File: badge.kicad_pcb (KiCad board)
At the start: 4 copper layers, 100 x 100 mm, 604 parts, among them IC1 SAMD21G18A-MU, J1 USB_C, J2 DEBUG, J3 LiPo 1S, Q1 3412, Q10 3412, Q11 3412, Q12 3412, Q13 3412, Q14 3412, Q15 3412, Q16 3412, Q2 3412, Q3 3412, Q4 3412, Q5 3412, Q6 3412, Q7 3412, Q8 3412, Q9 3412, SW1 A, SW2 B, SW3 X, SW4 Y, SW5 RESET, U1 74HC595, U2 74HC595, U3 TLC59025, U4 TLC59025, U5 GD25Q32C, U6 DW01, U7 TLV62569DBV, U8 PM8205A, U9 HX4054A, X1 #badgelife

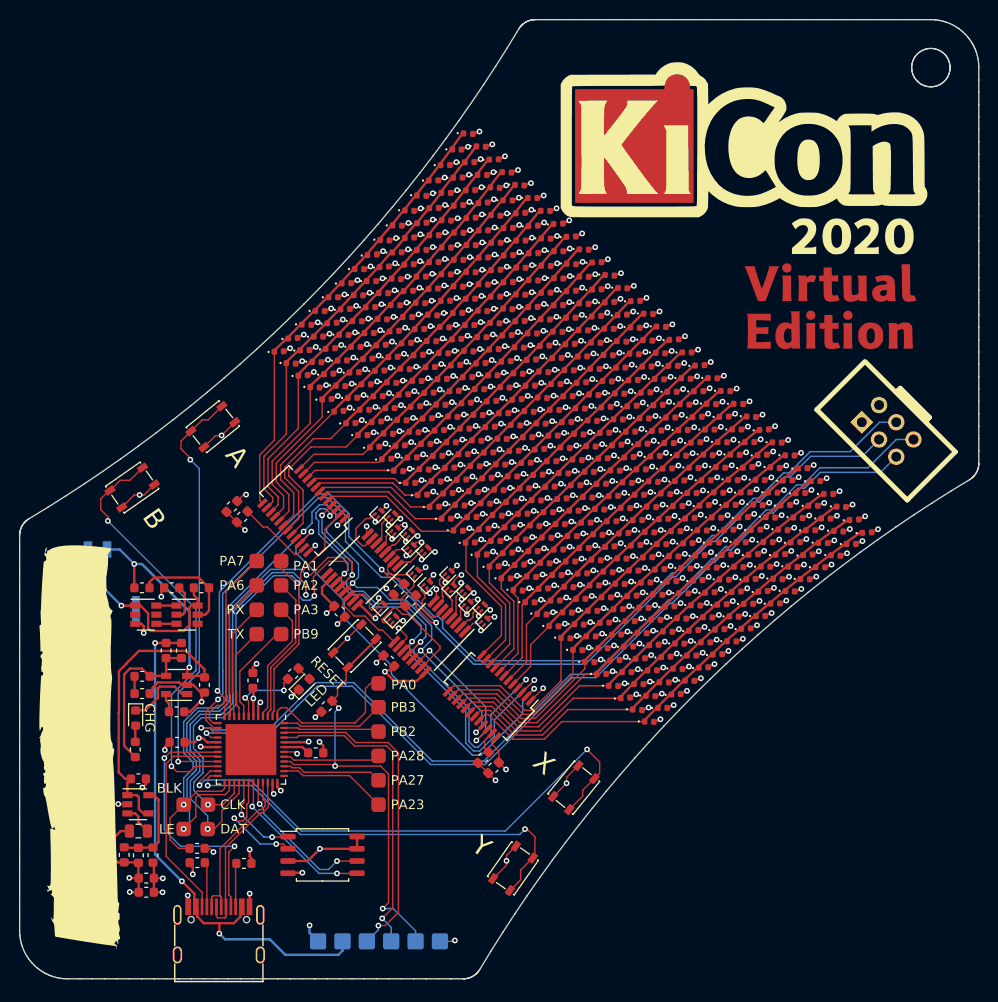
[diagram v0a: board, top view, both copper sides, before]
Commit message: Changed FETs to SOT-23 and buttons to something that is more boring
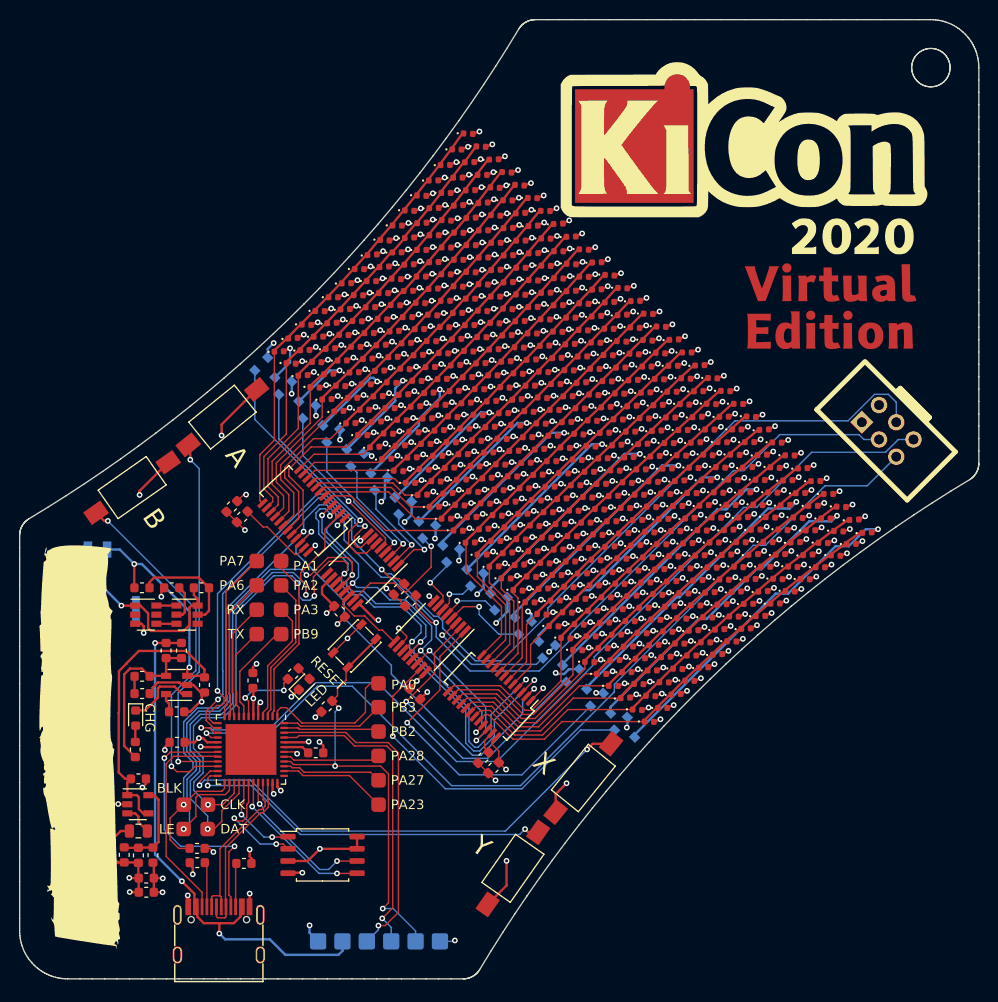
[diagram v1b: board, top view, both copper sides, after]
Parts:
- Q1, Q10, Q11, Q12, Q13, Q14, Q15, Q16, Q2, Q3, Q4, Q5, Q6, Q7, Q8, Q9: footprint Package_TO_SOT_SMD:SOT-883 -> Package_TO_SOT_SMD:SOT-23; moved to B.Cu
- R9: value 4.7K -> 4.7k
- SW1, SW2, SW3, SW4: footprint Button_Switch_SMD:SW_SPST_PTS810 -> tom-mechanical:SW_SPST_SMD_2PIN_3.5x6.0
- moved Q1 27.1 mm to (113.4, 124.1), turned to -45 degrees
- moved Q16 18.8 mm to (75.9, 86.6), turned to -45 degrees
- moved Q14 16.4 mm to (78.4, 89.1), turned to -45 degrees
- moved Q3 15.3 mm to (110.9, 121.6), turned to -45 degrees
- moved Q12 14.3 mm to (80.9, 91.6), turned to -45 degrees
- moved Q5 12.9 mm to (108.4, 119.1), turned to -45 degrees
- moved Q10 11.9 mm to (83.4, 94.1), turned to -45 degrees
- moved Q7 10.7 mm to (105.9, 116.6), turned to -45 degrees
- moved Q8 9.76 mm to (85.9, 96.6), turned to -45 degrees
- moved Q2 9.03 mm to (93.4, 104.1), turned to -45 degrees
- moved Q6 9.00 mm to (88.4, 99.1), turned to -45 degrees
- moved Q9 8.31 mm to (103.4, 114.1), turned to -45 degrees
- moved Q11 6.34 mm to (100.9, 111.6), turned to -45 degrees
- moved Q13 5.87 mm to (98.4, 109.1), turned to -45 degrees
- moved C2 4.39 mm to (91.2, 120.3), turned to -45 degrees
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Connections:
- net Net-(Q1-Pad1) renamed /ISSI 12 RGB A/U1_QA
- net Net-(Q10-Pad1) renamed /ISSI 12 RGB A/U2_QE
- net Net-(Q11-Pad1) renamed /ISSI 12 RGB A/U1_QF
- net Net-(Q12-Pad1) renamed /ISSI 12 RGB A/U2_QF
- net Net-(Q13-Pad1) renamed /ISSI 12 RGB A/U1_QG
- net Net-(Q14-Pad1) renamed /ISSI 12 RGB A/U2_QG
- net Net-(Q15-Pad1) renamed /ISSI 12 RGB A/U1_QH
- net Net-(Q16-Pad1) renamed /ISSI 12 RGB A/U2_QH
- net Net-(Q2-Pad1) renamed /ISSI 12 RGB A/U2_QA
- net Net-(Q3-Pad1) renamed /ISSI 12 RGB A/U1_QB
- net Net-(Q4-Pad1) renamed /ISSI 12 RGB A/U2_QB
- net Net-(Q5-Pad1) renamed /ISSI 12 RGB A/U1_QC
- net Net-(Q6-Pad1) renamed /ISSI 12 RGB A/U2_QC
- net Net-(Q7-Pad1) renamed /ISSI 12 RGB A/U1_QD
- net Net-(Q8-Pad1) renamed /ISSI 12 RGB A/U2_QD
- net Net-(Q9-Pad1) renamed /ISSI 12 RGB A/U1_QE
- D1 pad 2: /ISSI 12 RGB A/COM_6 -> /ISSI 12 RGB A/COM_2
- D10 pad 2: /ISSI 12 RGB A/COM_6 -> /ISSI 12 RGB A/COM_2
- D100 pad 2: /ISSI 12 RGB A/COM_2 -> /ISSI 12 RGB A/COM_1
- D101 pad 2: /ISSI 12 RGB A/COM_2 -> /ISSI 12 RGB A/COM_1
- D102 pad 2: /ISSI 12 RGB A/COM_2 -> /ISSI 12 RGB A/COM_1
- D103 pad 2: /ISSI 12 RGB A/COM_2 -> /ISSI 12 RGB A/COM_1
- D104 pad 2: /ISSI 12 RGB A/COM_2 -> /ISSI 12 RGB A/COM_1
- D105 pad 2: /ISSI 12 RGB A/COM_2 -> /ISSI 12 RGB A/COM_1
- D106 pad 2: /ISSI 12 RGB A/COM_2 -> /ISSI 12 RGB A/COM_1
- D107 pad 2: /ISSI 12 RGB A/COM_2 -> /ISSI 12 RGB A/COM_1
- D108 pad 2: /ISSI 12 RGB A/COM_2 -> /ISSI 12 RGB A/COM_1
- D109 pad 2: /ISSI 12 RGB A/COM_2 -> /ISSI 12 RGB A/COM_1
- D11 pad 2: /ISSI 12 RGB A/COM_6 -> /ISSI 12 RGB A/COM_2
- D110 pad 2: /ISSI 12 RGB A/COM_2 -> /ISSI 12 RGB A/COM_1
- D111 pad 2: /ISSI 12 RGB A/COM_2 -> /ISSI 12 RGB A/COM_1
- D112 pad 2: /ISSI 12 RGB A/COM_2 -> /ISSI 12 RGB A/COM_1
- D113 pad 2: /ISSI 12 RGB A/COM_2 -> /ISSI 12 RGB A/COM_1
- D114 pad 2: /ISSI 12 RGB A/COM_2 -> /ISSI 12 RGB A/COM_1
- D115 pad 2: /ISSI 12 RGB A/COM_2 -> /ISSI 12 RGB A/COM_1
- D116 pad 2: /ISSI 12 RGB A/COM_2 -> /ISSI 12 RGB A/COM_1
- D117 pad 2: /ISSI 12 RGB A/COM_2 -> /ISSI 12 RGB A/COM_1
- D118 pad 2: /ISSI 12 RGB A/COM_2 -> /ISSI 12 RGB A/COM_1
- D119 pad 2: /ISSI 12 RGB A/COM_2 -> /ISSI 12 RGB A/COM_1
- D12 pad 2: /ISSI 12 RGB A/COM_6 -> /ISSI 12 RGB A/COM_2
- D120 pad 2: /ISSI 12 RGB A/COM_2 -> /ISSI 12 RGB A/COM_1
- D121 pad 2: /ISSI 12 RGB A/COM_2 -> /ISSI 12 RGB A/COM_1
- D122 pad 2: /ISSI 12 RGB A/COM_2 -> /ISSI 12 RGB A/COM_1
- D123 pad 2: /ISSI 12 RGB A/COM_2 -> /ISSI 12 RGB A/COM_1
- D124 pad 2: /ISSI 12 RGB A/COM_2 -> /ISSI 12 RGB A/COM_1
- D125 pad 2: /ISSI 12 RGB A/COM_2 -> /ISSI 12 RGB A/COM_1
- D126 pad 2: /ISSI 12 RGB A/COM_2 -> /ISSI 12 RGB A/COM_1
- D127 pad 2: /ISSI 12 RGB A/COM_2 -> /ISSI 12 RGB A/COM_1
- D128 pad 2: /ISSI 12 RGB A/COM_2 -> /ISSI 12 RGB A/COM_1
- D129 pad 2: /ISSI 12 RGB A/COM_3 -> /ISSI 12 RGB A/COM
- D13 pad 2: /ISSI 12 RGB A/COM_6 -> /ISSI 12 RGB A/COM_2
- D130 pad 2: /ISSI 12 RGB A/COM_3 -> /ISSI 12 RGB A/COM
- D131 pad 2: /ISSI 12 RGB A/COM_3 -> /ISSI 12 RGB A/COM
- D132 pad 2: /ISSI 12 RGB A/COM_3 -> /ISSI 12 RGB A/COM
- D133 pad 2: /ISSI 12 RGB A/COM_3 -> /ISSI 12 RGB A/COM
- D134 pad 2: /ISSI 12 RGB A/COM_3 -> /ISSI 12 RGB A/COM
- D135 pad 2: /ISSI 12 RGB A/COM_3 -> /ISSI 12 RGB A/COM
- D136 pad 2: /ISSI 12 RGB A/COM_3 -> /ISSI 12 RGB A/COM
- D137 pad 2: /ISSI 12 RGB A/COM_3 -> /ISSI 12 RGB A/COM
- D138 pad 2: /ISSI 12 RGB A/COM_3 -> /ISSI 12 RGB A/COM
- D139 pad 2: /ISSI 12 RGB A/COM_3 -> /ISSI 12 RGB A/COM
- D14 pad 2: /ISSI 12 RGB A/COM_6 -> /ISSI 12 RGB A/COM_2
- D140 pad 2: /ISSI 12 RGB A/COM_3 -> /ISSI 12 RGB A/COM
- D141 pad 2: /ISSI 12 RGB A/COM_3 -> /ISSI 12 RGB A/COM
- D142 pad 2: /ISSI 12 RGB A/COM_3 -> /ISSI 12 RGB A/COM
- D143 pad 2: /ISSI 12 RGB A/COM_3 -> /ISSI 12 RGB A/COM
- D144 pad 2: /ISSI 12 RGB A/COM_3 -> /ISSI 12 RGB A/COM
- D145 pad 2: /ISSI 12 RGB A/COM_3 -> /ISSI 12 RGB A/COM
- D146 pad 2: /ISSI 12 RGB A/COM_3 -> /ISSI 12 RGB A/COM
- D147 pad 2: /ISSI 12 RGB A/COM_3 -> /ISSI 12 RGB A/COM
- D148 pad 2: /ISSI 12 RGB A/COM_3 -> /ISSI 12 RGB A/COM
- D149 pad 2: /ISSI 12 RGB A/COM_3 -> /ISSI 12 RGB A/COM
- D15 pad 2: /ISSI 12 RGB A/COM_6 -> /ISSI 12 RGB A/COM_2
- D150 pad 2: /ISSI 12 RGB A/COM_3 -> /ISSI 12 RGB A/COM
- D151 pad 2: /ISSI 12 RGB A/COM_3 -> /ISSI 12 RGB A/COM
- D152 pad 2: /ISSI 12 RGB A/COM_3 -> /ISSI 12 RGB A/COM
- D153 pad 2: /ISSI 12 RGB A/COM_3 -> /ISSI 12 RGB A/COM
- D154 pad 2: /ISSI 12 RGB A/COM_3 -> /ISSI 12 RGB A/COM
- D155 pad 2: /ISSI 12 RGB A/COM_3 -> /ISSI 12 RGB A/COM
- D156 pad 2: /ISSI 12 RGB A/COM_3 -> /ISSI 12 RGB A/COM
- D157 pad 2: /ISSI 12 RGB A/COM_3 -> /ISSI 12 RGB A/COM
- D158 pad 2: /ISSI 12 RGB A/COM_3 -> /ISSI 12 RGB A/COM
- D159 pad 2: /ISSI 12 RGB A/COM_3 -> /ISSI 12 RGB A/COM
- D16 pad 2: /ISSI 12 RGB A/COM_6 -> /ISSI 12 RGB A/COM_2
- D160 pad 2: /ISSI 12 RGB A/COM_3 -> /ISSI 12 RGB A/COM
- D161 pad 2: /ISSI 12 RGB A/COM_8 -> /ISSI 12 RGB A/COM_14
- D162 pad 2: /ISSI 12 RGB A/COM_8 -> /ISSI 12 RGB A/COM_14
- D163 pad 2: /ISSI 12 RGB A/COM_8 -> /ISSI 12 RGB A/COM_14
- D164 pad 2: /ISSI 12 RGB A/COM_8 -> /ISSI 12 RGB A/COM_14
- D165 pad 2: /ISSI 12 RGB A/COM_8 -> /ISSI 12 RGB A/COM_14
- D166 pad 2: /ISSI 12 RGB A/COM_8 -> /ISSI 12 RGB A/COM_14
- D167 pad 2: /ISSI 12 RGB A/COM_8 -> /ISSI 12 RGB A/COM_14
- D168 pad 2: /ISSI 12 RGB A/COM_8 -> /ISSI 12 RGB A/COM_14
- D169 pad 2: /ISSI 12 RGB A/COM_8 -> /ISSI 12 RGB A/COM_14
- D17 pad 2: /ISSI 12 RGB A/COM_6 -> /ISSI 12 RGB A/COM_2
- D170 pad 2: /ISSI 12 RGB A/COM_8 -> /ISSI 12 RGB A/COM_14
- D171 pad 2: /ISSI 12 RGB A/COM_8 -> /ISSI 12 RGB A/COM_14
- D172 pad 2: /ISSI 12 RGB A/COM_8 -> /ISSI 12 RGB A/COM_14
- D173 pad 2: /ISSI 12 RGB A/COM_8 -> /ISSI 12 RGB A/COM_14
- D174 pad 2: /ISSI 12 RGB A/COM_8 -> /ISSI 12 RGB A/COM_14
- D175 pad 2: /ISSI 12 RGB A/COM_8 -> /ISSI 12 RGB A/COM_14
- D176 pad 2: /ISSI 12 RGB A/COM_8 -> /ISSI 12 RGB A/COM_14
- D177 pad 2: /ISSI 12 RGB A/COM_8 -> /ISSI 12 RGB A/COM_14
- D178 pad 2: /ISSI 12 RGB A/COM_8 -> /ISSI 12 RGB A/COM_14
- D179 pad 2: /ISSI 12 RGB A/COM_8 -> /ISSI 12 RGB A/COM_14
- D18 pad 2: /ISSI 12 RGB A/COM_6 -> /ISSI 12 RGB A/COM_2
- D180 pad 2: /ISSI 12 RGB A/COM_8 -> /ISSI 12 RGB A/COM_14
- D181 pad 2: /ISSI 12 RGB A/COM_8 -> /ISSI 12 RGB A/COM_14
- D182 pad 2: /ISSI 12 RGB A/COM_8 -> /ISSI 12 RGB A/COM_14
- D183 pad 2: /ISSI 12 RGB A/COM_8 -> /ISSI 12 RGB A/COM_14
- D184 pad 2: /ISSI 12 RGB A/COM_8 -> /ISSI 12 RGB A/COM_14
- D185 pad 2: /ISSI 12 RGB A/COM_8 -> /ISSI 12 RGB A/COM_14
- D186 pad 2: /ISSI 12 RGB A/COM_8 -> /ISSI 12 RGB A/COM_14
- D187 pad 2: /ISSI 12 RGB A/COM_8 -> /ISSI 12 RGB A/COM_14
- D188 pad 2: /ISSI 12 RGB A/COM_8 -> /ISSI 12 RGB A/COM_14
- D189 pad 2: /ISSI 12 RGB A/COM_8 -> /ISSI 12 RGB A/COM_14
- D19 pad 2: /ISSI 12 RGB A/COM_6 -> /ISSI 12 RGB A/COM_2
- D190 pad 2: /ISSI 12 RGB A/COM_8 -> /ISSI 12 RGB A/COM_14
- D191 pad 2: /ISSI 12 RGB A/COM_8 -> /ISSI 12 RGB A/COM_14
- D192 pad 2: /ISSI 12 RGB A/COM_8 -> /ISSI 12 RGB A/COM_14
- D193 pad 2: /ISSI 12 RGB A/COM_14 -> /ISSI 12 RGB A/COM_13
- D194 pad 2: /ISSI 12 RGB A/COM_14 -> /ISSI 12 RGB A/COM_13
- D195 pad 2: /ISSI 12 RGB A/COM_14 -> /ISSI 12 RGB A/COM_13
- D196 pad 2: /ISSI 12 RGB A/COM_14 -> /ISSI 12 RGB A/COM_13
- D197 pad 2: /ISSI 12 RGB A/COM_14 -> /ISSI 12 RGB A/COM_13
- D198 pad 2: /ISSI 12 RGB A/COM_14 -> /ISSI 12 RGB A/COM_13
- D199 pad 2: /ISSI 12 RGB A/COM_14 -> /ISSI 12 RGB A/COM_13
- D2 pad 2: /ISSI 12 RGB A/COM_6 -> /ISSI 12 RGB A/COM_2
- D20 pad 2: /ISSI 12 RGB A/COM_6 -> /ISSI 12 RGB A/COM_2
- D200 pad 2: /ISSI 12 RGB A/COM_14 -> /ISSI 12 RGB A/COM_13
- D201 pad 2: /ISSI 12 RGB A/COM_14 -> /ISSI 12 RGB A/COM_13
- D202 pad 2: /ISSI 12 RGB A/COM_14 -> /ISSI 12 RGB A/COM_13
- D203 pad 2: /ISSI 12 RGB A/COM_14 -> /ISSI 12 RGB A/COM_13
- D204 pad 2: /ISSI 12 RGB A/COM_14 -> /ISSI 12 RGB A/COM_13
- D205 pad 2: /ISSI 12 RGB A/COM_14 -> /ISSI 12 RGB A/COM_13
- D206 pad 2: /ISSI 12 RGB A/COM_14 -> /ISSI 12 RGB A/COM_13
- D207 pad 2: /ISSI 12 RGB A/COM_14 -> /ISSI 12 RGB A/COM_13
- D208 pad 2: /ISSI 12 RGB A/COM_14 -> /ISSI 12 RGB A/COM_13
- D209 pad 2: /ISSI 12 RGB A/COM_14 -> /ISSI 12 RGB A/COM_13
- D21 pad 2: /ISSI 12 RGB A/COM_6 -> /ISSI 12 RGB A/COM_2
- D210 pad 2: /ISSI 12 RGB A/COM_14 -> /ISSI 12 RGB A/COM_13
- D211 pad 2: /ISSI 12 RGB A/COM_14 -> /ISSI 12 RGB A/COM_13
- D212 pad 2: /ISSI 12 RGB A/COM_14 -> /ISSI 12 RGB A/COM_13
- D213 pad 2: /ISSI 12 RGB A/COM_14 -> /ISSI 12 RGB A/COM_13
- D214 pad 2: /ISSI 12 RGB A/COM_14 -> /ISSI 12 RGB A/COM_13
- D215 pad 2: /ISSI 12 RGB A/COM_14 -> /ISSI 12 RGB A/COM_13
- D216 pad 2: /ISSI 12 RGB A/COM_14 -> /ISSI 12 RGB A/COM_13
- D217 pad 2: /ISSI 12 RGB A/COM_14 -> /ISSI 12 RGB A/COM_13
- D218 pad 2: /ISSI 12 RGB A/COM_14 -> /ISSI 12 RGB A/COM_13
- D219 pad 2: /ISSI 12 RGB A/COM_14 -> /ISSI 12 RGB A/COM_13
- D22 pad 2: /ISSI 12 RGB A/COM_6 -> /ISSI 12 RGB A/COM_2
- D220 pad 2: /ISSI 12 RGB A/COM_14 -> /ISSI 12 RGB A/COM_13
- D221 pad 2: /ISSI 12 RGB A/COM_14 -> /ISSI 12 RGB A/COM_13
- D222 pad 2: /ISSI 12 RGB A/COM_14 -> /ISSI 12 RGB A/COM_13
- D223 pad 2: /ISSI 12 RGB A/COM_14 -> /ISSI 12 RGB A/COM_13
- D224 pad 2: /ISSI 12 RGB A/COM_14 -> /ISSI 12 RGB A/COM_13
- D225 pad 2: /ISSI 12 RGB A/COM_1 -> /ISSI 12 RGB A/COM_15
- D226 pad 2: /ISSI 12 RGB A/COM_1 -> /ISSI 12 RGB A/COM_15
- D227 pad 2: /ISSI 12 RGB A/COM_1 -> /ISSI 12 RGB A/COM_15
- D228 pad 2: /ISSI 12 RGB A/COM_1 -> /ISSI 12 RGB A/COM_15
- D229 pad 2: /ISSI 12 RGB A/COM_1 -> /ISSI 12 RGB A/COM_15
- D23 pad 2: /ISSI 12 RGB A/COM_6 -> /ISSI 12 RGB A/COM_2
- D230 pad 2: /ISSI 12 RGB A/COM_1 -> /ISSI 12 RGB A/COM_15
- D231 pad 2: /ISSI 12 RGB A/COM_1 -> /ISSI 12 RGB A/COM_15
- D232 pad 2: /ISSI 12 RGB A/COM_1 -> /ISSI 12 RGB A/COM_15
- D233 pad 2: /ISSI 12 RGB A/COM_1 -> /ISSI 12 RGB A/COM_15
- D234 pad 2: /ISSI 12 RGB A/COM_1 -> /ISSI 12 RGB A/COM_15
- D235 pad 2: /ISSI 12 RGB A/COM_1 -> /ISSI 12 RGB A/COM_15
- D236 pad 2: /ISSI 12 RGB A/COM_1 -> /ISSI 12 RGB A/COM_15
- D237 pad 2: /ISSI 12 RGB A/COM_1 -> /ISSI 12 RGB A/COM_15
- D238 pad 2: /ISSI 12 RGB A/COM_1 -> /ISSI 12 RGB A/COM_15
- D239 pad 2: /ISSI 12 RGB A/COM_1 -> /ISSI 12 RGB A/COM_15
- D24 pad 2: /ISSI 12 RGB A/COM_6 -> /ISSI 12 RGB A/COM_2
- D240 pad 2: /ISSI 12 RGB A/COM_1 -> /ISSI 12 RGB A/COM_15
- D241 pad 2: /ISSI 12 RGB A/COM_1 -> /ISSI 12 RGB A/COM_15
- D242 pad 2: /ISSI 12 RGB A/COM_1 -> /ISSI 12 RGB A/COM_15
- D243 pad 2: /ISSI 12 RGB A/COM_1 -> /ISSI 12 RGB A/COM_15
- D244 pad 2: /ISSI 12 RGB A/COM_1 -> /ISSI 12 RGB A/COM_15
- D245 pad 2: /ISSI 12 RGB A/COM_1 -> /ISSI 12 RGB A/COM_15
- D246 pad 2: /ISSI 12 RGB A/COM_1 -> /ISSI 12 RGB A/COM_15
- D247 pad 2: /ISSI 12 RGB A/COM_1 -> /ISSI 12 RGB A/COM_15
- D248 pad 2: /ISSI 12 RGB A/COM_1 -> /ISSI 12 RGB A/COM_15
- D249 pad 2: /ISSI 12 RGB A/COM_1 -> /ISSI 12 RGB A/COM_15
- D25 pad 2: /ISSI 12 RGB A/COM_6 -> /ISSI 12 RGB A/COM_2
- D250 pad 2: /ISSI 12 RGB A/COM_1 -> /ISSI 12 RGB A/COM_15
- D251 pad 2: /ISSI 12 RGB A/COM_1 -> /ISSI 12 RGB A/COM_15
- D252 pad 2: /ISSI 12 RGB A/COM_1 -> /ISSI 12 RGB A/COM_15
- D253 pad 2: /ISSI 12 RGB A/COM_1 -> /ISSI 12 RGB A/COM_15
- D254 pad 2: /ISSI 12 RGB A/COM_1 -> /ISSI 12 RGB A/COM_15
- D255 pad 2: /ISSI 12 RGB A/COM_1 -> /ISSI 12 RGB A/COM_15
- D256 pad 2: /ISSI 12 RGB A/COM_1 -> /ISSI 12 RGB A/COM_15
- D257 pad 2: /ISSI 12 RGB A/COM_7 -> /ISSI 12 RGB A/COM_5
- D258 pad 2: /ISSI 12 RGB A/COM_7 -> /ISSI 12 RGB A/COM_5
- D259 pad 2: /ISSI 12 RGB A/COM_7 -> /ISSI 12 RGB A/COM_5
- D26 pad 2: /ISSI 12 RGB A/COM_6 -> /ISSI 12 RGB A/COM_2
- D260 pad 2: /ISSI 12 RGB A/COM_7 -> /ISSI 12 RGB A/COM_5
- D261 pad 2: /ISSI 12 RGB A/COM_7 -> /ISSI 12 RGB A/COM_5
- D262 pad 2: /ISSI 12 RGB A/COM_7 -> /ISSI 12 RGB A/COM_5
- D263 pad 2: /ISSI 12 RGB A/COM_7 -> /ISSI 12 RGB A/COM_5
- D264 pad 2: /ISSI 12 RGB A/COM_7 -> /ISSI 12 RGB A/COM_5
- D265 pad 2: /ISSI 12 RGB A/COM_7 -> /ISSI 12 RGB A/COM_5
- D266 pad 2: /ISSI 12 RGB A/COM_7 -> /ISSI 12 RGB A/COM_5
- D267 pad 2: /ISSI 12 RGB A/COM_7 -> /ISSI 12 RGB A/COM_5
- D268 pad 2: /ISSI 12 RGB A/COM_7 -> /ISSI 12 RGB A/COM_5
- D269 pad 2: /ISSI 12 RGB A/COM_7 -> /ISSI 12 RGB A/COM_5
- D27 pad 2: /ISSI 12 RGB A/COM_6 -> /ISSI 12 RGB A/COM_2
- D270 pad 2: /ISSI 12 RGB A/COM_7 -> /ISSI 12 RGB A/COM_5
- D271 pad 2: /ISSI 12 RGB A/COM_7 -> /ISSI 12 RGB A/COM_5
- D272 pad 2: /ISSI 12 RGB A/COM_7 -> /ISSI 12 RGB A/COM_5
- D273 pad 2: /ISSI 12 RGB A/COM_7 -> /ISSI 12 RGB A/COM_5
- D274 pad 2: /ISSI 12 RGB A/COM_7 -> /ISSI 12 RGB A/COM_5
- D275 pad 2: /ISSI 12 RGB A/COM_7 -> /ISSI 12 RGB A/COM_5
- D276 pad 2: /ISSI 12 RGB A/COM_7 -> /ISSI 12 RGB A/COM_5
- D277 pad 2: /ISSI 12 RGB A/COM_7 -> /ISSI 12 RGB A/COM_5
- D278 pad 2: /ISSI 12 RGB A/COM_7 -> /ISSI 12 RGB A/COM_5
- D279 pad 2: /ISSI 12 RGB A/COM_7 -> /ISSI 12 RGB A/COM_5
- D28 pad 2: /ISSI 12 RGB A/COM_6 -> /ISSI 12 RGB A/COM_2
- D280 pad 2: /ISSI 12 RGB A/COM_7 -> /ISSI 12 RGB A/COM_5
- D281 pad 2: /ISSI 12 RGB A/COM_7 -> /ISSI 12 RGB A/COM_5
- D282 pad 2: /ISSI 12 RGB A/COM_7 -> /ISSI 12 RGB A/COM_5
- D283 pad 2: /ISSI 12 RGB A/COM_7 -> /ISSI 12 RGB A/COM_5
- D284 pad 2: /ISSI 12 RGB A/COM_7 -> /ISSI 12 RGB A/COM_5
- D285 pad 2: /ISSI 12 RGB A/COM_7 -> /ISSI 12 RGB A/COM_5
- D286 pad 2: /ISSI 12 RGB A/COM_7 -> /ISSI 12 RGB A/COM_5
- D287 pad 2: /ISSI 12 RGB A/COM_7 -> /ISSI 12 RGB A/COM_5
- D288 pad 2: /ISSI 12 RGB A/COM_7 -> /ISSI 12 RGB A/COM_5
- D289 pad 2: /ISSI 12 RGB A/COM_15 -> /ISSI 12 RGB A/COM_6
- D29 pad 2: /ISSI 12 RGB A/COM_6 -> /ISSI 12 RGB A/COM_2
- D290 pad 2: /ISSI 12 RGB A/COM_15 -> /ISSI 12 RGB A/COM_6
- D291 pad 2: /ISSI 12 RGB A/COM_15 -> /ISSI 12 RGB A/COM_6
- D292 pad 2: /ISSI 12 RGB A/COM_15 -> /ISSI 12 RGB A/COM_6
- D293 pad 2: /ISSI 12 RGB A/COM_15 -> /ISSI 12 RGB A/COM_6
- D294 pad 2: /ISSI 12 RGB A/COM_15 -> /ISSI 12 RGB A/COM_6
- D295 pad 2: /ISSI 12 RGB A/COM_15 -> /ISSI 12 RGB A/COM_6
- D296 pad 2: /ISSI 12 RGB A/COM_15 -> /ISSI 12 RGB A/COM_6
- D297 pad 2: /ISSI 12 RGB A/COM_15 -> /ISSI 12 RGB A/COM_6
- D298 pad 2: /ISSI 12 RGB A/COM_15 -> /ISSI 12 RGB A/COM_6
- D299 pad 2: /ISSI 12 RGB A/COM_15 -> /ISSI 12 RGB A/COM_6
- D3 pad 2: /ISSI 12 RGB A/COM_6 -> /ISSI 12 RGB A/COM_2
- D30 pad 2: /ISSI 12 RGB A/COM_6 -> /ISSI 12 RGB A/COM_2
- D300 pad 2: /ISSI 12 RGB A/COM_15 -> /ISSI 12 RGB A/COM_6
- D301 pad 2: /ISSI 12 RGB A/COM_15 -> /ISSI 12 RGB A/COM_6
- D302 pad 2: /ISSI 12 RGB A/COM_15 -> /ISSI 12 RGB A/COM_6
- D303 pad 2: /ISSI 12 RGB A/COM_15 -> /ISSI 12 RGB A/COM_6
- D304 pad 2: /ISSI 12 RGB A/COM_15 -> /ISSI 12 RGB A/COM_6
- D305 pad 2: /ISSI 12 RGB A/COM_15 -> /ISSI 12 RGB A/COM_6
- D306 pad 2: /ISSI 12 RGB A/COM_15 -> /ISSI 12 RGB A/COM_6
- D307 pad 2: /ISSI 12 RGB A/COM_15 -> /ISSI 12 RGB A/COM_6
- D308 pad 2: /ISSI 12 RGB A/COM_15 -> /ISSI 12 RGB A/COM_6
- D309 pad 2: /ISSI 12 RGB A/COM_15 -> /ISSI 12 RGB A/COM_6
- D31 pad 2: /ISSI 12 RGB A/COM_6 -> /ISSI 12 RGB A/COM_2
- D310 pad 2: /ISSI 12 RGB A/COM_15 -> /ISSI 12 RGB A/COM_6
- D311 pad 2: /ISSI 12 RGB A/COM_15 -> /ISSI 12 RGB A/COM_6
- D312 pad 2: /ISSI 12 RGB A/COM_15 -> /ISSI 12 RGB A/COM_6
- D313 pad 2: /ISSI 12 RGB A/COM_15 -> /ISSI 12 RGB A/COM_6
- D314 pad 2: /ISSI 12 RGB A/COM_15 -> /ISSI 12 RGB A/COM_6
- D315 pad 2: /ISSI 12 RGB A/COM_15 -> /ISSI 12 RGB A/COM_6
- D316 pad 2: /ISSI 12 RGB A/COM_15 -> /ISSI 12 RGB A/COM_6
- D317 pad 2: /ISSI 12 RGB A/COM_15 -> /ISSI 12 RGB A/COM_6
- D318 pad 2: /ISSI 12 RGB A/COM_15 -> /ISSI 12 RGB A/COM_6
- D319 pad 2: /ISSI 12 RGB A/COM_15 -> /ISSI 12 RGB A/COM_6
- D32 pad 2: /ISSI 12 RGB A/COM_6 -> /ISSI 12 RGB A/COM_2
- D320 pad 2: /ISSI 12 RGB A/COM_15 -> /ISSI 12 RGB A/COM_6
- D321 pad 2: /ISSI 12 RGB A/COM -> /ISSI 12 RGB A/COM_7
- D322 pad 2: /ISSI 12 RGB A/COM -> /ISSI 12 RGB A/COM_7
- D323 pad 2: /ISSI 12 RGB A/COM -> /ISSI 12 RGB A/COM_7
- D324 pad 2: /ISSI 12 RGB A/COM -> /ISSI 12 RGB A/COM_7
- D325 pad 2: /ISSI 12 RGB A/COM -> /ISSI 12 RGB A/COM_7
- D326 pad 2: /ISSI 12 RGB A/COM -> /ISSI 12 RGB A/COM_7
- D327 pad 2: /ISSI 12 RGB A/COM -> /ISSI 12 RGB A/COM_7
- D328 pad 2: /ISSI 12 RGB A/COM -> /ISSI 12 RGB A/COM_7
- D329 pad 2: /ISSI 12 RGB A/COM -> /ISSI 12 RGB A/COM_7
- D33 pad 2: /ISSI 12 RGB A/COM_5 -> /ISSI 12 RGB A/COM_3
- D330 pad 2: /ISSI 12 RGB A/COM -> /ISSI 12 RGB A/COM_7
- D331 pad 2: /ISSI 12 RGB A/COM -> /ISSI 12 RGB A/COM_7
- D332 pad 2: /ISSI 12 RGB A/COM -> /ISSI 12 RGB A/COM_7
- D333 pad 2: /ISSI 12 RGB A/COM -> /ISSI 12 RGB A/COM_7
- D334 pad 2: /ISSI 12 RGB A/COM -> /ISSI 12 RGB A/COM_7
- D335 pad 2: /ISSI 12 RGB A/COM -> /ISSI 12 RGB A/COM_7
- D336 pad 2: /ISSI 12 RGB A/COM -> /ISSI 12 RGB A/COM_7
- D337 pad 2: /ISSI 12 RGB A/COM -> /ISSI 12 RGB A/COM_7
- D338 pad 2: /ISSI 12 RGB A/COM -> /ISSI 12 RGB A/COM_7
- D339 pad 2: /ISSI 12 RGB A/COM -> /ISSI 12 RGB A/COM_7
- D34 pad 2: /ISSI 12 RGB A/COM_5 -> /ISSI 12 RGB A/COM_3
- D340 pad 2: /ISSI 12 RGB A/COM -> /ISSI 12 RGB A/COM_7
- D341 pad 2: /ISSI 12 RGB A/COM -> /ISSI 12 RGB A/COM_7
- D342 pad 2: /ISSI 12 RGB A/COM -> /ISSI 12 RGB A/COM_7
- D343 pad 2: /ISSI 12 RGB A/COM -> /ISSI 12 RGB A/COM_7
- D344 pad 2: /ISSI 12 RGB A/COM -> /ISSI 12 RGB A/COM_7
- D345 pad 2: /ISSI 12 RGB A/COM -> /ISSI 12 RGB A/COM_7
- D346 pad 2: /ISSI 12 RGB A/COM -> /ISSI 12 RGB A/COM_7
- D347 pad 2: /ISSI 12 RGB A/COM -> /ISSI 12 RGB A/COM_7
- D348 pad 2: /ISSI 12 RGB A/COM -> /ISSI 12 RGB A/COM_7
- D349 pad 2: /ISSI 12 RGB A/COM -> /ISSI 12 RGB A/COM_7
- D35 pad 2: /ISSI 12 RGB A/COM_5 -> /ISSI 12 RGB A/COM_3
- D350 pad 2: /ISSI 12 RGB A/COM -> /ISSI 12 RGB A/COM_7
- D351 pad 2: /ISSI 12 RGB A/COM -> /ISSI 12 RGB A/COM_7
- D352 pad 2: /ISSI 12 RGB A/COM -> /ISSI 12 RGB A/COM_7
- D353 pad 2: /ISSI 12 RGB A/COM_12 -> /ISSI 12 RGB A/COM_8
- D354 pad 2: /ISSI 12 RGB A/COM_12 -> /ISSI 12 RGB A/COM_8
- D355 pad 2: /ISSI 12 RGB A/COM_12 -> /ISSI 12 RGB A/COM_8
- D356 pad 2: /ISSI 12 RGB A/COM_12 -> /ISSI 12 RGB A/COM_8
- D357 pad 2: /ISSI 12 RGB A/COM_12 -> /ISSI 12 RGB A/COM_8
- D358 pad 2: /ISSI 12 RGB A/COM_12 -> /ISSI 12 RGB A/COM_8
- D359 pad 2: /ISSI 12 RGB A/COM_12 -> /ISSI 12 RGB A/COM_8
- D36 pad 2: /ISSI 12 RGB A/COM_5 -> /ISSI 12 RGB A/COM_3
- D360 pad 2: /ISSI 12 RGB A/COM_12 -> /ISSI 12 RGB A/COM_8
- D361 pad 2: /ISSI 12 RGB A/COM_12 -> /ISSI 12 RGB A/COM_8
- D362 pad 2: /ISSI 12 RGB A/COM_12 -> /ISSI 12 RGB A/COM_8
- D363 pad 2: /ISSI 12 RGB A/COM_12 -> /ISSI 12 RGB A/COM_8
- D364 pad 2: /ISSI 12 RGB A/COM_12 -> /ISSI 12 RGB A/COM_8
- D365 pad 2: /ISSI 12 RGB A/COM_12 -> /ISSI 12 RGB A/COM_8
- D366 pad 2: /ISSI 12 RGB A/COM_12 -> /ISSI 12 RGB A/COM_8
- D367 pad 2: /ISSI 12 RGB A/COM_12 -> /ISSI 12 RGB A/COM_8
- D368 pad 2: /ISSI 12 RGB A/COM_12 -> /ISSI 12 RGB A/COM_8
- D369 pad 2: /ISSI 12 RGB A/COM_12 -> /ISSI 12 RGB A/COM_8
- D37 pad 2: /ISSI 12 RGB A/COM_5 -> /ISSI 12 RGB A/COM_3
- D370 pad 2: /ISSI 12 RGB A/COM_12 -> /ISSI 12 RGB A/COM_8
- D371 pad 2: /ISSI 12 RGB A/COM_12 -> /ISSI 12 RGB A/COM_8
- D372 pad 2: /ISSI 12 RGB A/COM_12 -> /ISSI 12 RGB A/COM_8
- D373 pad 2: /ISSI 12 RGB A/COM_12 -> /ISSI 12 RGB A/COM_8
- D374 pad 2: /ISSI 12 RGB A/COM_12 -> /ISSI 12 RGB A/COM_8
- D375 pad 2: /ISSI 12 RGB A/COM_12 -> /ISSI 12 RGB A/COM_8
- D376 pad 2: /ISSI 12 RGB A/COM_12 -> /ISSI 12 RGB A/COM_8
- D377 pad 2: /ISSI 12 RGB A/COM_12 -> /ISSI 12 RGB A/COM_8
- D378 pad 2: /ISSI 12 RGB A/COM_12 -> /ISSI 12 RGB A/COM_8
- D379 pad 2: /ISSI 12 RGB A/COM_12 -> /ISSI 12 RGB A/COM_8
- D38 pad 2: /ISSI 12 RGB A/COM_5 -> /ISSI 12 RGB A/COM_3
- D380 pad 2: /ISSI 12 RGB A/COM_12 -> /ISSI 12 RGB A/COM_8
- D381 pad 2: /ISSI 12 RGB A/COM_12 -> /ISSI 12 RGB A/COM_8
- D382 pad 2: /ISSI 12 RGB A/COM_12 -> /ISSI 12 RGB A/COM_8
- D383 pad 2: /ISSI 12 RGB A/COM_12 -> /ISSI 12 RGB A/COM_8
- D384 pad 2: /ISSI 12 RGB A/COM_12 -> /ISSI 12 RGB A/COM_8
- D385 pad 2: /ISSI 12 RGB A/COM_13 -> /ISSI 12 RGB A/COM_9
- D386 pad 2: /ISSI 12 RGB A/COM_13 -> /ISSI 12 RGB A/COM_9
- D387 pad 2: /ISSI 12 RGB A/COM_13 -> /ISSI 12 RGB A/COM_9
- D388 pad 2: /ISSI 12 RGB A/COM_13 -> /ISSI 12 RGB A/COM_9
- D389 pad 2: /ISSI 12 RGB A/COM_13 -> /ISSI 12 RGB A/COM_9
- D39 pad 2: /ISSI 12 RGB A/COM_5 -> /ISSI 12 RGB A/COM_3
- D390 pad 2: /ISSI 12 RGB A/COM_13 -> /ISSI 12 RGB A/COM_9
- D391 pad 2: /ISSI 12 RGB A/COM_13 -> /ISSI 12 RGB A/COM_9
- D392 pad 2: /ISSI 12 RGB A/COM_13 -> /ISSI 12 RGB A/COM_9
- D393 pad 2: /ISSI 12 RGB A/COM_13 -> /ISSI 12 RGB A/COM_9
- D394 pad 2: /ISSI 12 RGB A/COM_13 -> /ISSI 12 RGB A/COM_9
- D395 pad 2: /ISSI 12 RGB A/COM_13 -> /ISSI 12 RGB A/COM_9
- D396 pad 2: /ISSI 12 RGB A/COM_13 -> /ISSI 12 RGB A/COM_9
- D397 pad 2: /ISSI 12 RGB A/COM_13 -> /ISSI 12 RGB A/COM_9
- D398 pad 2: /ISSI 12 RGB A/COM_13 -> /ISSI 12 RGB A/COM_9
- D399 pad 2: /ISSI 12 RGB A/COM_13 -> /ISSI 12 RGB A/COM_9
- D4 pad 2: /ISSI 12 RGB A/COM_6 -> /ISSI 12 RGB A/COM_2
- D40 pad 2: /ISSI 12 RGB A/COM_5 -> /ISSI 12 RGB A/COM_3
- D400 pad 2: /ISSI 12 RGB A/COM_13 -> /ISSI 12 RGB A/COM_9
- D401 pad 2: /ISSI 12 RGB A/COM_13 -> /ISSI 12 RGB A/COM_9
- D402 pad 2: /ISSI 12 RGB A/COM_13 -> /ISSI 12 RGB A/COM_9
- D403 pad 2: /ISSI 12 RGB A/COM_13 -> /ISSI 12 RGB A/COM_9
- D404 pad 2: /ISSI 12 RGB A/COM_13 -> /ISSI 12 RGB A/COM_9
- D405 pad 2: /ISSI 12 RGB A/COM_13 -> /ISSI 12 RGB A/COM_9
- D406 pad 2: /ISSI 12 RGB A/COM_13 -> /ISSI 12 RGB A/COM_9
- D407 pad 2: /ISSI 12 RGB A/COM_13 -> /ISSI 12 RGB A/COM_9
- D408 pad 2: /ISSI 12 RGB A/COM_13 -> /ISSI 12 RGB A/COM_9
- D409 pad 2: /ISSI 12 RGB A/COM_13 -> /ISSI 12 RGB A/COM_9
- D41 pad 2: /ISSI 12 RGB A/COM_5 -> /ISSI 12 RGB A/COM_3
- D410 pad 2: /ISSI 12 RGB A/COM_13 -> /ISSI 12 RGB A/COM_9
- D411 pad 2: /ISSI 12 RGB A/COM_13 -> /ISSI 12 RGB A/COM_9
- D412 pad 2: /ISSI 12 RGB A/COM_13 -> /ISSI 12 RGB A/COM_9
- D413 pad 2: /ISSI 12 RGB A/COM_13 -> /ISSI 12 RGB A/COM_9
- D414 pad 2: /ISSI 12 RGB A/COM_13 -> /ISSI 12 RGB A/COM_9
- D415 pad 2: /ISSI 12 RGB A/COM_13 -> /ISSI 12 RGB A/COM_9
- D416 pad 2: /ISSI 12 RGB A/COM_13 -> /ISSI 12 RGB A/COM_9
- D417 pad 2: /ISSI 12 RGB A/COM_9 -> /ISSI 12 RGB A/COM_10
- D418 pad 2: /ISSI 12 RGB A/COM_9 -> /ISSI 12 RGB A/COM_10
- D419 pad 2: /ISSI 12 RGB A/COM_9 -> /ISSI 12 RGB A/COM_10
- D42 pad 2: /ISSI 12 RGB A/COM_5 -> /ISSI 12 RGB A/COM_3
- D420 pad 2: /ISSI 12 RGB A/COM_9 -> /ISSI 12 RGB A/COM_10
- D421 pad 2: /ISSI 12 RGB A/COM_9 -> /ISSI 12 RGB A/COM_10
- D422 pad 2: /ISSI 12 RGB A/COM_9 -> /ISSI 12 RGB A/COM_10
- D423 pad 2: /ISSI 12 RGB A/COM_9 -> /ISSI 12 RGB A/COM_10
- D424 pad 2: /ISSI 12 RGB A/COM_9 -> /ISSI 12 RGB A/COM_10
- D425 pad 2: /ISSI 12 RGB A/COM_9 -> /ISSI 12 RGB A/COM_10
- D426 pad 2: /ISSI 12 RGB A/COM_9 -> /ISSI 12 RGB A/COM_10
- D427 pad 2: /ISSI 12 RGB A/COM_9 -> /ISSI 12 RGB A/COM_10
- D428 pad 2: /ISSI 12 RGB A/COM_9 -> /ISSI 12 RGB A/COM_10
- D429 pad 2: /ISSI 12 RGB A/COM_9 -> /ISSI 12 RGB A/COM_10
- D43 pad 2: /ISSI 12 RGB A/COM_5 -> /ISSI 12 RGB A/COM_3
- D430 pad 2: /ISSI 12 RGB A/COM_9 -> /ISSI 12 RGB A/COM_10
- D431 pad 2: /ISSI 12 RGB A/COM_9 -> /ISSI 12 RGB A/COM_10
- D432 pad 2: /ISSI 12 RGB A/COM_9 -> /ISSI 12 RGB A/COM_10
- D433 pad 2: /ISSI 12 RGB A/COM_9 -> /ISSI 12 RGB A/COM_10
- D434 pad 2: /ISSI 12 RGB A/COM_9 -> /ISSI 12 RGB A/COM_10
- D435 pad 2: /ISSI 12 RGB A/COM_9 -> /ISSI 12 RGB A/COM_10
- D436 pad 2: /ISSI 12 RGB A/COM_9 -> /ISSI 12 RGB A/COM_10
- D437 pad 2: /ISSI 12 RGB A/COM_9 -> /ISSI 12 RGB A/COM_10
- D438 pad 2: /ISSI 12 RGB A/COM_9 -> /ISSI 12 RGB A/COM_10
- D439 pad 2: /ISSI 12 RGB A/COM_9 -> /ISSI 12 RGB A/COM_10
- D44 pad 2: /ISSI 12 RGB A/COM_5 -> /ISSI 12 RGB A/COM_3
- D440 pad 2: /ISSI 12 RGB A/COM_9 -> /ISSI 12 RGB A/COM_10
- D441 pad 2: /ISSI 12 RGB A/COM_9 -> /ISSI 12 RGB A/COM_10
- D442 pad 2: /ISSI 12 RGB A/COM_9 -> /ISSI 12 RGB A/COM_10
- D443 pad 2: /ISSI 12 RGB A/COM_9 -> /ISSI 12 RGB A/COM_10
- D444 pad 2: /ISSI 12 RGB A/COM_9 -> /ISSI 12 RGB A/COM_10
- D445 pad 2: /ISSI 12 RGB A/COM_9 -> /ISSI 12 RGB A/COM_10
- D446 pad 2: /ISSI 12 RGB A/COM_9 -> /ISSI 12 RGB A/COM_10
- D447 pad 2: /ISSI 12 RGB A/COM_9 -> /ISSI 12 RGB A/COM_10
- D448 pad 2: /ISSI 12 RGB A/COM_9 -> /ISSI 12 RGB A/COM_10
- D449 pad 2: /ISSI 12 RGB A/COM_10 -> /ISSI 12 RGB A/COM_11
- D45 pad 2: /ISSI 12 RGB A/COM_5 -> /ISSI 12 RGB A/COM_3
- D450 pad 2: /ISSI 12 RGB A/COM_10 -> /ISSI 12 RGB A/COM_11
- D451 pad 2: /ISSI 12 RGB A/COM_10 -> /ISSI 12 RGB A/COM_11
- D452 pad 2: /ISSI 12 RGB A/COM_10 -> /ISSI 12 RGB A/COM_11
- D453 pad 2: /ISSI 12 RGB A/COM_10 -> /ISSI 12 RGB A/COM_11
- D454 pad 2: /ISSI 12 RGB A/COM_10 -> /ISSI 12 RGB A/COM_11
- D455 pad 2: /ISSI 12 RGB A/COM_10 -> /ISSI 12 RGB A/COM_11
- D456 pad 2: /ISSI 12 RGB A/COM_10 -> /ISSI 12 RGB A/COM_11
- D457 pad 2: /ISSI 12 RGB A/COM_10 -> /ISSI 12 RGB A/COM_11
- D458 pad 2: /ISSI 12 RGB A/COM_10 -> /ISSI 12 RGB A/COM_11
- D459 pad 2: /ISSI 12 RGB A/COM_10 -> /ISSI 12 RGB A/COM_11
- D46 pad 2: /ISSI 12 RGB A/COM_5 -> /ISSI 12 RGB A/COM_3
- D460 pad 2: /ISSI 12 RGB A/COM_10 -> /ISSI 12 RGB A/COM_11
- D461 pad 2: /ISSI 12 RGB A/COM_10 -> /ISSI 12 RGB A/COM_11
- D462 pad 2: /ISSI 12 RGB A/COM_10 -> /ISSI 12 RGB A/COM_11
- D463 pad 2: /ISSI 12 RGB A/COM_10 -> /ISSI 12 RGB A/COM_11
- D464 pad 2: /ISSI 12 RGB A/COM_10 -> /ISSI 12 RGB A/COM_11
- D465 pad 2: /ISSI 12 RGB A/COM_10 -> /ISSI 12 RGB A/COM_11
- D466 pad 2: /ISSI 12 RGB A/COM_10 -> /ISSI 12 RGB A/COM_11
- D467 pad 2: /ISSI 12 RGB A/COM_10 -> /ISSI 12 RGB A/COM_11
- D468 pad 2: /ISSI 12 RGB A/COM_10 -> /ISSI 12 RGB A/COM_11
- D469 pad 2: /ISSI 12 RGB A/COM_10 -> /ISSI 12 RGB A/COM_11
- D47 pad 2: /ISSI 12 RGB A/COM_5 -> /ISSI 12 RGB A/COM_3
- D470 pad 2: /ISSI 12 RGB A/COM_10 -> /ISSI 12 RGB A/COM_11
- D471 pad 2: /ISSI 12 RGB A/COM_10 -> /ISSI 12 RGB A/COM_11
- D472 pad 2: /ISSI 12 RGB A/COM_10 -> /ISSI 12 RGB A/COM_11
- D473 pad 2: /ISSI 12 RGB A/COM_10 -> /ISSI 12 RGB A/COM_11
- D474 pad 2: /ISSI 12 RGB A/COM_10 -> /ISSI 12 RGB A/COM_11
- D475 pad 2: /ISSI 12 RGB A/COM_10 -> /ISSI 12 RGB A/COM_11
- D476 pad 2: /ISSI 12 RGB A/COM_10 -> /ISSI 12 RGB A/COM_11
- D477 pad 2: /ISSI 12 RGB A/COM_10 -> /ISSI 12 RGB A/COM_11
- D478 pad 2: /ISSI 12 RGB A/COM_10 -> /ISSI 12 RGB A/COM_11
- D479 pad 2: /ISSI 12 RGB A/COM_10 -> /ISSI 12 RGB A/COM_11
- D48 pad 2: /ISSI 12 RGB A/COM_5 -> /ISSI 12 RGB A/COM_3
- D480 pad 2: /ISSI 12 RGB A/COM_10 -> /ISSI 12 RGB A/COM_11
- D481 pad 2: /ISSI 12 RGB A/COM_11 -> /ISSI 12 RGB A/COM_12
- D482 pad 2: /ISSI 12 RGB A/COM_11 -> /ISSI 12 RGB A/COM_12
- D483 pad 2: /ISSI 12 RGB A/COM_11 -> /ISSI 12 RGB A/COM_12
- D484 pad 2: /ISSI 12 RGB A/COM_11 -> /ISSI 12 RGB A/COM_12
- D485 pad 2: /ISSI 12 RGB A/COM_11 -> /ISSI 12 RGB A/COM_12
- D486 pad 2: /ISSI 12 RGB A/COM_11 -> /ISSI 12 RGB A/COM_12
- D487 pad 2: /ISSI 12 RGB A/COM_11 -> /ISSI 12 RGB A/COM_12
- D488 pad 2: /ISSI 12 RGB A/COM_11 -> /ISSI 12 RGB A/COM_12
- D489 pad 2: /ISSI 12 RGB A/COM_11 -> /ISSI 12 RGB A/COM_12
- D49 pad 2: /ISSI 12 RGB A/COM_5 -> /ISSI 12 RGB A/COM_3
- D490 pad 2: /ISSI 12 RGB A/COM_11 -> /ISSI 12 RGB A/COM_12
- D491 pad 2: /ISSI 12 RGB A/COM_11 -> /ISSI 12 RGB A/COM_12
- D492 pad 2: /ISSI 12 RGB A/COM_11 -> /ISSI 12 RGB A/COM_12
- D493 pad 2: /ISSI 12 RGB A/COM_11 -> /ISSI 12 RGB A/COM_12
- D494 pad 2: /ISSI 12 RGB A/COM_11 -> /ISSI 12 RGB A/COM_12
- D495 pad 2: /ISSI 12 RGB A/COM_11 -> /ISSI 12 RGB A/COM_12
- D496 pad 2: /ISSI 12 RGB A/COM_11 -> /ISSI 12 RGB A/COM_12
- D497 pad 2: /ISSI 12 RGB A/COM_11 -> /ISSI 12 RGB A/COM_12
- D498 pad 2: /ISSI 12 RGB A/COM_11 -> /ISSI 12 RGB A/COM_12
- D499 pad 2: /ISSI 12 RGB A/COM_11 -> /ISSI 12 RGB A/COM_12
- D5 pad 2: /ISSI 12 RGB A/COM_6 -> /ISSI 12 RGB A/COM_2
- D50 pad 2: /ISSI 12 RGB A/COM_5 -> /ISSI 12 RGB A/COM_3
- D500 pad 2: /ISSI 12 RGB A/COM_11 -> /ISSI 12 RGB A/COM_12
- D501 pad 2: /ISSI 12 RGB A/COM_11 -> /ISSI 12 RGB A/COM_12
- D502 pad 2: /ISSI 12 RGB A/COM_11 -> /ISSI 12 RGB A/COM_12
- D503 pad 2: /ISSI 12 RGB A/COM_11 -> /ISSI 12 RGB A/COM_12
- D504 pad 2: /ISSI 12 RGB A/COM_11 -> /ISSI 12 RGB A/COM_12
- D505 pad 2: /ISSI 12 RGB A/COM_11 -> /ISSI 12 RGB A/COM_12
- D506 pad 2: /ISSI 12 RGB A/COM_11 -> /ISSI 12 RGB A/COM_12
- D507 pad 2: /ISSI 12 RGB A/COM_11 -> /ISSI 12 RGB A/COM_12
- D508 pad 2: /ISSI 12 RGB A/COM_11 -> /ISSI 12 RGB A/COM_12
- D509 pad 2: /ISSI 12 RGB A/COM_11 -> /ISSI 12 RGB A/COM_12
- D51 pad 2: /ISSI 12 RGB A/COM_5 -> /ISSI 12 RGB A/COM_3
- D510 pad 2: /ISSI 12 RGB A/COM_11 -> /ISSI 12 RGB A/COM_12
- D511 pad 2: /ISSI 12 RGB A/COM_11 -> /ISSI 12 RGB A/COM_12
- D512 pad 2: /ISSI 12 RGB A/COM_11 -> /ISSI 12 RGB A/COM_12
- D52 pad 2: /ISSI 12 RGB A/COM_5 -> /ISSI 12 RGB A/COM_3
- D53 pad 2: /ISSI 12 RGB A/COM_5 -> /ISSI 12 RGB A/COM_3
- D54 pad 2: /ISSI 12 RGB A/COM_5 -> /ISSI 12 RGB A/COM_3
- D55 pad 2: /ISSI 12 RGB A/COM_5 -> /ISSI 12 RGB A/COM_3
- D56 pad 2: /ISSI 12 RGB A/COM_5 -> /ISSI 12 RGB A/COM_3
- D57 pad 2: /ISSI 12 RGB A/COM_5 -> /ISSI 12 RGB A/COM_3
- D58 pad 2: /ISSI 12 RGB A/COM_5 -> /ISSI 12 RGB A/COM_3
- D59 pad 2: /ISSI 12 RGB A/COM_5 -> /ISSI 12 RGB A/COM_3
- D6 pad 2: /ISSI 12 RGB A/COM_6 -> /ISSI 12 RGB A/COM_2
- D60 pad 2: /ISSI 12 RGB A/COM_5 -> /ISSI 12 RGB A/COM_3
- D61 pad 2: /ISSI 12 RGB A/COM_5 -> /ISSI 12 RGB A/COM_3
- D62 pad 2: /ISSI 12 RGB A/COM_5 -> /ISSI 12 RGB A/COM_3
- D63 pad 2: /ISSI 12 RGB A/COM_5 -> /ISSI 12 RGB A/COM_3
- D64 pad 2: /ISSI 12 RGB A/COM_5 -> /ISSI 12 RGB A/COM_3
- D7 pad 2: /ISSI 12 RGB A/COM_6 -> /ISSI 12 RGB A/COM_2
- D8 pad 2: /ISSI 12 RGB A/COM_6 -> /ISSI 12 RGB A/COM_2
- D9 pad 2: /ISSI 12 RGB A/COM_6 -> /ISSI 12 RGB A/COM_2
- D97 pad 2: /ISSI 12 RGB A/COM_2 -> /ISSI 12 RGB A/COM_1
- D98 pad 2: /ISSI 12 RGB A/COM_2 -> /ISSI 12 RGB A/COM_1
- D99 pad 2: /ISSI 12 RGB A/COM_2 -> /ISSI 12 RGB A/COM_1
- IC1 pad 37: (no net) -> /SAMD21/SDB
- Q1 pad 3: /ISSI 12 RGB A/COM_6 -> /ISSI 12 RGB A/COM_2
- Q10 pad 3: /ISSI 12 RGB A/COM_13 -> /ISSI 12 RGB A/COM_9
- Q11 pad 3: /ISSI 12 RGB A/COM_8 -> /ISSI 12 RGB A/COM_14
- Q12 pad 3: /ISSI 12 RGB A/COM_9 -> /ISSI 12 RGB A/COM_10
- Q13 pad 3: /ISSI 12 RGB A/COM_14 -> /ISSI 12 RGB A/COM_13
- Q14 pad 3: /ISSI 12 RGB A/COM_10 -> /ISSI 12 RGB A/COM_11
- Q15 pad 3: /ISSI 12 RGB A/COM_1 -> /ISSI 12 RGB A/COM_15
- Q16 pad 3: /ISSI 12 RGB A/COM_11 -> /ISSI 12 RGB A/COM_12
- Q2 pad 3: /ISSI 12 RGB A/COM_7 -> /ISSI 12 RGB A/COM_5
- Q3 pad 3: /ISSI 12 RGB A/COM_5 -> /ISSI 12 RGB A/COM_3
- Q4 pad 3: /ISSI 12 RGB A/COM_15 -> /ISSI 12 RGB A/COM_6
- Q6 pad 3: /ISSI 12 RGB A/COM -> /ISSI 12 RGB A/COM_7
- Q7 pad 3: /ISSI 12 RGB A/COM_2 -> /ISSI 12 RGB A/COM_1
- Q8 pad 3: /ISSI 12 RGB A/COM_12 -> /ISSI 12 RGB A/COM_8
- Q9 pad 3: /ISSI 12 RGB A/COM_3 -> /ISSI 12 RGB A/COM
- U2 pad 9: (no net) -> Net-(U2-Pad9)
- U6 pad 4: (no net) -> Net-(U6-Pad4)
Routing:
- net /ISSI 12 RGB A/U1_QB: track 2.11 -> 36.3 mm, vias 0 -> 1
- net /ISSI 12 RGB A/COM_6: track 126.0 -> 94.0 mm, vias 33 -> 32
- net /ISSI 12 RGB A/U1_QC: track 2.97 -> 32.3 mm, vias 0 -> 1
- net /ISSI 12 RGB A/U1_QA: track 12.4 -> 36.3 mm, vias 0 -> 1
- net /ISSI 12 RGB A/COM_5: track 116.7 -> 96.6 mm, vias 33 -> 32
- net /ISSI 12 RGB A/U2_QH: track 6.02 -> 26.1 mm, vias 0 -> 1
- net /ISSI 12 RGB A/U2_QG: track 3.32 -> 23.4 mm, vias 0 -> 1
- net /ISSI 12 RGB A/COM_8: track 105.7 -> 89.9 mm, vias 33 -> 32
- net /ISSI 12 RGB A/COM_7: track 106.9 -> 91.8 mm, vias 33 -> 32
- net /ISSI 12 RGB A/U2_QF: track 2.23 -> 17.3 mm, vias 0 -> 1
- net /ISSI 12 RGB A/U1_QD: track 2.22 -> 14.0 mm, vias 0 -> 1
- net /ISSI 12 RGB A/U2_QE: track 2.98 -> 14.7 mm, vias 0 -> 1
- net /ISSI 12 RGB A/COM_13: track 90.2 -> 101.3 mm, vias 33 -> 32
- net /ISSI 12 RGB A/COM: track 96.1 -> 106.3 mm, vias 33 -> 32
- net /ISSI 12 RGB A/COM_12: track 92.2 -> 82.0 mm, vias 33 -> 32
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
